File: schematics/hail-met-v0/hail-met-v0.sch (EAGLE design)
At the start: 87 parts, among them IC1 MCP73871, J1 AVR_SPI_PRG_6PTH, U1 ATMEGA328P, Y1 16MHZ

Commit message: finished initial schematic and routing, updated software pin assignment
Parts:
- removed ATM_PB, ATM_PC, ATM_PD, ATM_PWR, JP4: (no value), SparkFun-Connectors:M08LOCK
- removed LED7-FREE: M02PTH, SparkFun-Connectors:M02PTH
- added AND-GATE: SN74ALVC08PWR, Texas Instruments_By_element14_Batch_1:SN74ALVC08PWR
- added AT_PINS: M04X2, SparkFun-Connectors:M04X2
- added JP-BT1, JP-BT2, JP-BT3: (no value), SparkFun-Connectors:M04LOCK
- added LED7-CS, LED_CHG, LED_DONE, LED_LB, SW_BSEL1, SW_BSEL2, SW_TL1, SW_TR1: M02PTH, SparkFun-Connectors:M02PTH
- added NOT-GATE: SN74LVC3G14DCTR, Texas Instruments_By_element14_Batch_1:SN74LVC3G14DCTR
- added R14, R15: (no value), SparkFun-Passives:RESISTOR0805-RES
- renumbered JP3 to JP-BT0
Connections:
- net CHG_PWR renamed N$29
- removed net A: U1.PC1(ADC1)
- removed net B: U1.PC2(ADC2)
- removed net BT_DISC: U1.PD4(XCK/T0)
- removed net BT_GPIO10: JP4.8, U$3.GPIO10
- removed net BT_GPIO2: JP4.1
- removed net BT_GPIO5: JP4.4, U$3.GPIO5
- removed net BT_GPIO9: JP4.7
- removed net BT_PAIR: U1.PD7(AIN1)
- removed net C: U1.PC3(ADC3)
- removed net N$15: ATM_PC.1, ATM_PD.1
- removed net N$16: ATM_PC.2, ATM_PD.2
- removed net N$23: DONE.A, R5.1
- removed net N$26: ATM_PC.3, ATM_PD.3
- removed net N$32: ATM_PC.4, ATM_PD.4
- removed net N$34: U1.ADC7
- removed net N$43: ATM_PC.5, ATM_PD.5, ATM_PWR.5
- removed net N$45: ATM_PC.6, ATM_PD.6, ATM_PWR.6
- removed net N$46: ATM_PC.7, ATM_PD.7, ATM_PWR.7
- removed net N$47: ATM_PC.8, ATM_PD.8, ATM_PWR.8
- removed net N$48: ATM_PB.1
- removed net N$49: ATM_PB.2
- removed net N$50: ATM_PB.3
- removed net N$51: ATM_PB.4
- removed net N$52: ATM_PB.5
- removed net N$53: ATM_PB.6
- removed net N$54: ATM_PB.7
- removed net N$55: ATM_PB.8
- removed net N$67: LED_CREE.2, R24.1
- removed net SW_BFF: SW_BFF.1
- removed net SW_BRR: SW_BRR.1
- removed net SW_BSEL: SW_BSEL.1
- new net ADC6: AT_PINS.2, U1.ADC6
- new net ADC7: AT_PINS.4, U1.ADC7
- new net BT_NEXT: SW_BSEL1.1, U$3.GPIO11
- new net BT_PLAY: SW_BSEL.1, U$3.GPIO13
- new net BT_PREV: SW_BSEL2.1, U$3.GPIO12
- new net BT_USBD+: JP-BT1.3, U$3.USBD+
- new net BT_USBD-: JP-BT1.2, U$3.USBD-
- new net BT_VOL_DN: SW_BRR.1, U$3.GPIO10
- new net BT_VOL_UP: SW_BFF.1, U$3.GPIO5
- new net CHG_CHARGING: AND-GATE.4Y, LED_CHG.1
- new net CHG_LOWBATT: AND-GATE.3Y, LED_LB.1
- new net CHG_PG: AND-GATE.3B, NOT-GATE.3A, PWR.A, R6.1
- new net CHG_STAT2: AND-GATE.2B, DONE.A, NOT-GATE.2A, R5.1
- new net N$20: CHRG/LBO.C, IC1.STAT1/LBO
- new net N$28: DONE.C, IC1.STAT2
- new net N$30: LED_CHG.2, R24.1
- new net PC1: AT_PINS.3, U1.PC1(ADC1)
- new net PC2: AT_PINS.5, U1.PC2(ADC2)
- new net PC3: AT_PINS.7, U1.PC3(ADC3)
- new net STAT12: AND-GATE.2Y, AND-GATE.3A, AND-GATE.4A
- new net SW_BT_DISC: SW_TL1.1, U1.PD4(XCK/T0)
- new net SW_CALL: SW_TR1.1
- new net ~CHG_PG: AND-GATE.4B, NOT-GATE.3Y
- new net ~CHG_STAT1: AND-GATE.2A, NOT-GATE.1Y
- new net ~CHG_STAT2: AND-GATE.1B, NOT-GATE.2Y
- net 3.3V: now also AND-GATE.VCC, AT_PINS.1, JP-BT2.4, LED7-CS.1, NOT-GATE.VCC, R13.2, R5.2, R6.2; no longer LED7-FREE.1
- net AMB_IN: now also U1.PC0(ADC0); no longer U1.ADC6
- net BT_CONN: now also U1.PD7(AIN1); no longer U1.PD5(T1)
- net BT_GPIO3: now also JP-BT1.1; no longer JP4.2
- net BT_GPIO4: now also JP-BT2.1; no longer JP4.3
- net BT_GPIO6: now also JP-BT2.2; no longer JP4.5
- net BT_GPIO7: now also JP-BT2.3; no longer JP4.6
- net CHG_DONE: now also AND-GATE.1Y, LED_DONE.1; no longer DONE.C, IC1.STAT2
- net CHG_STAT1: now also AND-GATE.1A, CHRG/LBO.A, NOT-GATE.1A, R13.1; no longer CHRG/LBO.C, IC1.STAT1/LBO
- net CHG_VOUT: now also JP-BT3.1; no longer ATM_PWR.1, C7.1, U$1.IN
- net EXT_5V: now also JP-BT3.3; no longer ATM_PWR.3
- net GND: now also AND-GATE.GND, AT_PINS.6, AT_PINS.8, JP-BT1.4, JP-BT3.4, NOT-GATE.GND, R14.2, R15.2, R24.2, SW_BSEL1.2, SW_BSEL2.2, SW_TL1.2, SW_TR1.2; no longer ATM_PWR.4
- net LED_CREE: now also U1.PD5(T1); no longer U1.PC0(ADC0)
- net N$19: now also LED_CREE.2; no longer R24.2
- net N$22: now also LED_DONE.2, R14.1; no longer CHRG/LBO.A, R13.1
- net N$24: now also LED_LB.2, R15.1; no longer PWR.A, R6.1
- net N$61: now also LED7-CS.2; no longer LED7-FREE.2
- net VCHG: no longer R13.2, R5.2, R6.2
- net VIN: now also C7.1, JP-BT3.2, U$1.IN; no longer ATM_PWR.2
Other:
- note added: "A0"
- note added: "A1"
- note added: "A2"
- note added: "A3"
- note added: "A4"
- note added: "A5"
- note added: "Breakout for ATmega328P"
- note added: "D0"
- note added: "D1"
- note added: "D10"
- note added: "D11"
- note added: "D12"
- note added: "D13"
- note added: "D2"
- note added: "D3"
- note added: "D4"
- note added: "D5"
- note added: "D6"
- note added: "D7"
- note added: "D8"
- note added: "D9"
- note added: "Logic for charge status LEDs"
- note added: "Names: ------ LED0-LF Left Front LED0-IL Indicator Left LED1-LM Left Middle LED2-LR Left Rear LED3-HR Headlight Rear LED4-RF Right Front LED4-IR Indicator Right LED5-RM Right Middle LED6-RR Right Rear LED7-CS Call Status"
- note added: "Names: ------ SW_TL Turn Left SW_TR Turn Right SW_BT_DISC Bluetooth Discoverable SW_CALL Accept/Reject call"
- note added: "See Fig 2-4 for usage http://ww1.microchip.com/downloads/ en/DeviceDoc/rn-52-ds-1.1r.pdf"
- note added: "x"
- note removed: "Breakout for ATmega328"
- note removed: "Do we need these jumpers?"
- note removed: "Names: ------ LED0-LF Left Front LED0-IL Indicator Left LED1-LM Left Middle LED2-LR Left Rear LED3-HR Headlight Front LED4-RF Right Front LED4-IR Indicator Right LED5-RM Right Middle LED6-RR Right Rear LED7-FREE"
- note removed: "Names: ------ SW-TL Turn Left SW-TR Turn Right SW-BFF Bluetooth Fast Forward SW-BRR Bluetooth Rewind SW-BSEL Bluetooth Select"
- note removed: "Note: Processor pins do not match button pins yet, and pins and there is 1 less pin than expected. ADC6/ ADC7 were factored in as pins, but not on standard Arduino IDE(?)"
- moved on the sheet: C1, CHRG/LBO, DONE, FTDI, J1, LED0-IL, LED0-IR, LED0-LF, LED1-LM, LED2-LR, LED3-HR, LED4-RF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

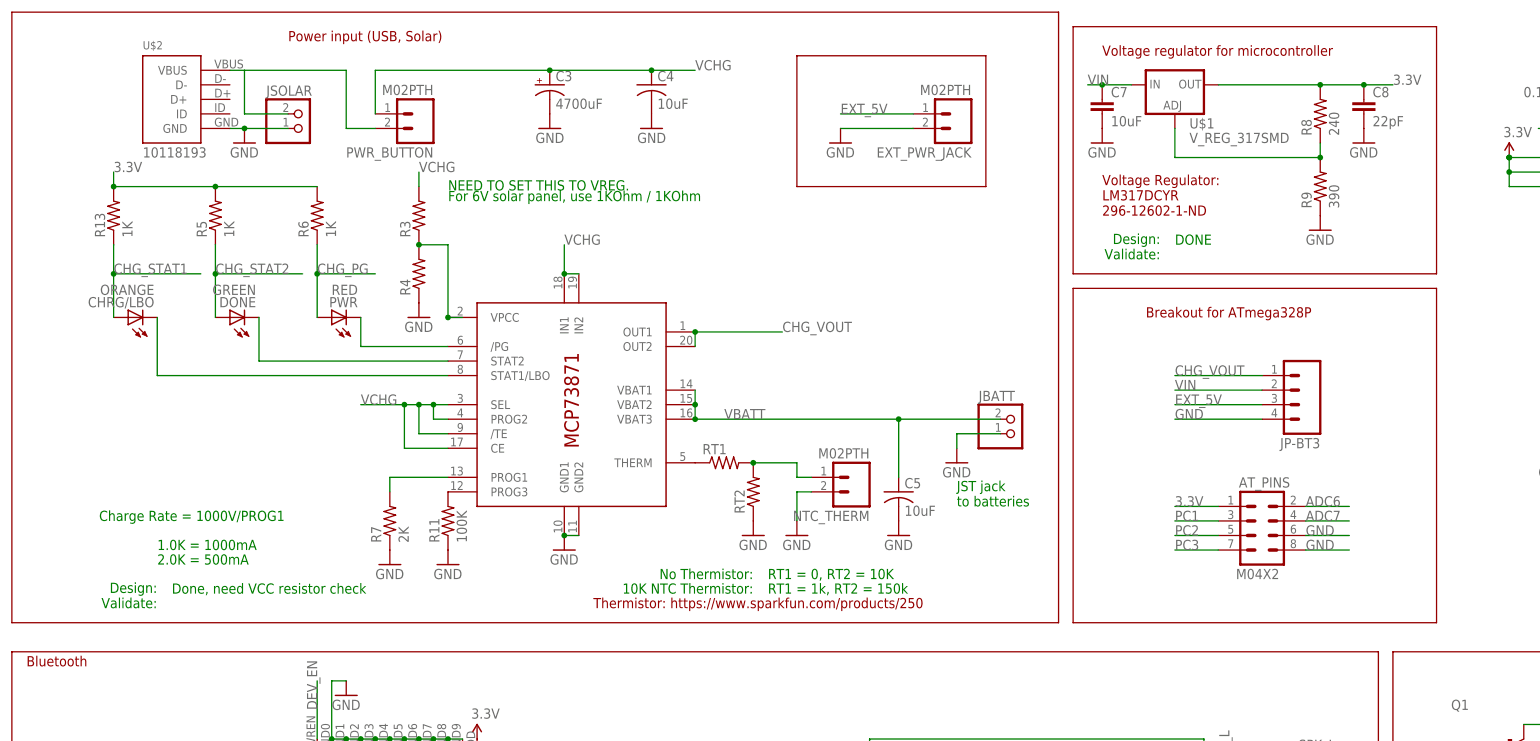
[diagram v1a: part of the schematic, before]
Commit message: added some power planes
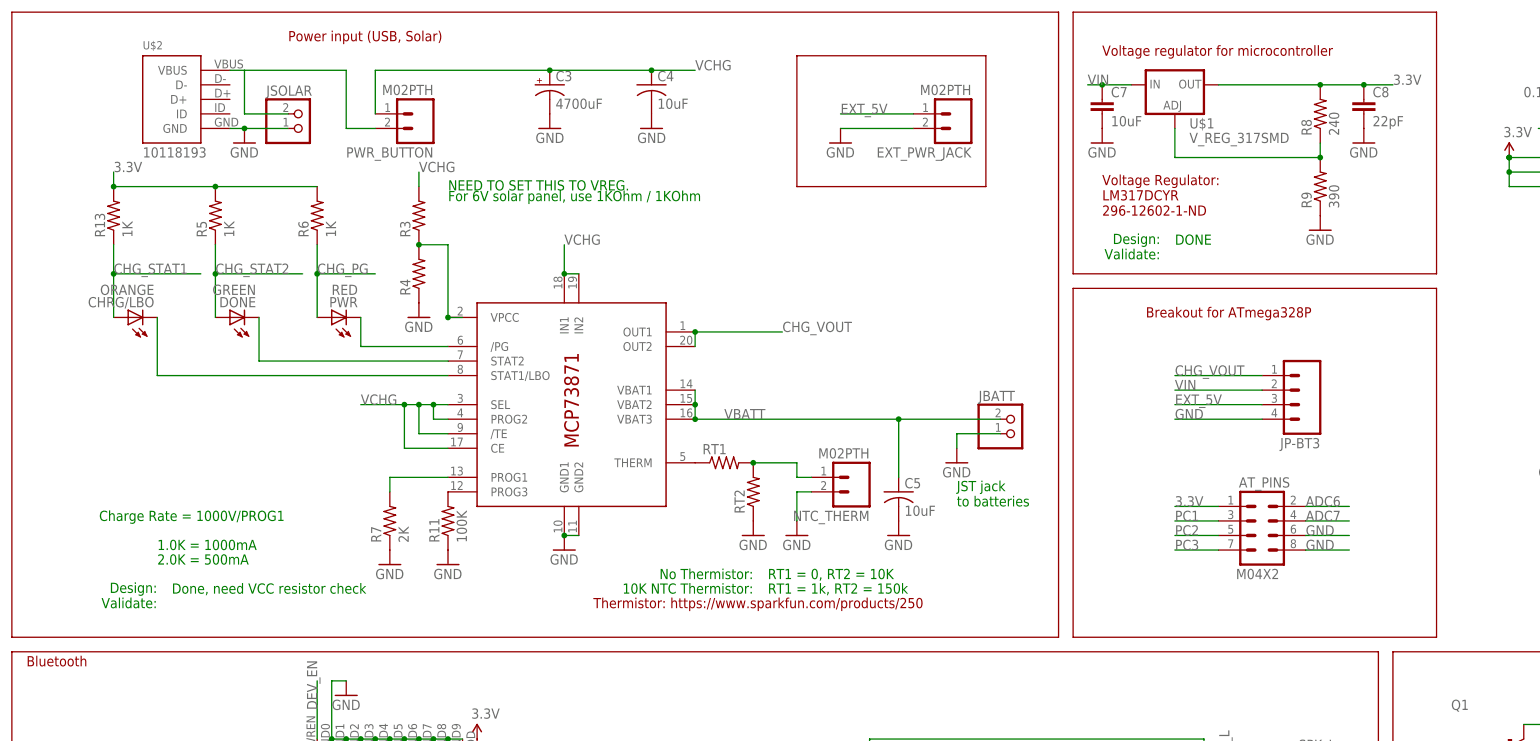
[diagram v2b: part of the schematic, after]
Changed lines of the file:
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@@
 <text x="2.54" y="96.52" size="1.778" layer="94">Voltage regulator for microcontroller</text>
 <text x="81.28" y="-33.02" size="1.778" layer="94">LED Driver</text>
-<wire x1="-187.96" y1="104.14" x2="-187.96" y2="-2.54" width="0.1524" layer="94"/>
-<wire x1="-187.96" y1="-2.54" x2="-5.08" y2="-2.54" width="0.1524" layer="94"/>
-<wire x1="-5.08" y1="-2.54" x2="-5.08" y2="104.14" width="0.1524" layer="94"/>
+<wire x1="-187.96" y1="104.14" x2="-187.96" y2="-5.08" width="0.1524" layer="94"/>
+<wire x1="-187.96" y1="-5.08" x2="-5.08" y2="-5.08" width="0.1524" layer="94"/>
+<wire x1="-5.08" y1="-5.08" x2="-5.08" y2="104.14" width="0.1524" layer="94"/>
 <wire x1="-5.08" y1="104.14" x2="-187.96" y2="104.14" width="0.1524" layer="94"/>
 <text x="-139.7" y="99.06" size="1.778" layer="94">Power input (USB, Solar)</text>
@@
 For 6V solar panel, use 1KOhm / 1KOhm</text>
 <text x="15.24" y="63.5" size="1.778" layer="91">DONE</text>
-<wire x1="-2.54" y1="101.6" x2="60.96" y2="101.6" width="0.1524" layer="94"/>
-<wire x1="60.96" y1="101.6" x2="60.96" y2="58.42" width="0.1524" layer="94"/>
+<wire x1="-2.54" y1="104.14" x2="60.96" y2="104.14" width="0.1524" layer="94"/>
+<wire x1="60.96" y1="104.14" x2="60.96" y2="58.42" width="0.1524" layer="94"/>
 <wire x1="60.96" y1="58.42" x2="-2.54" y2="58.42" width="0.1524" layer="94"/>
-<wire x1="-2.54" y1="58.42" x2="-2.54" y2="101.6" width="0.1524" layer="94"/>
+<wire x1="-2.54" y1="58.42" x2="-2.54" y2="104.14" width="0.1524" layer="94"/>
 <text x="12.7" y="60.96" size="1.778" layer="91" align="bottom-right">Design:
 Validate:</text>
@@
 <wire x1="304.8" y1="-101.6" x2="304.8" y2="-7.62" width="0.1524" layer="94"/>
 <wire x1="304.8" y1="-7.62" x2="223.52" y2="-7.62" width="0.1524" layer="94"/>
-<wire x1="-2.54" y1="55.88" x2="-2.54" y2="-2.54" width="0.1524" layer="94"/>
-<wire x1="-2.54" y1="-2.54" x2="60.96" y2="-2.54" width="0.1524" layer="94"/>
-<wire x1="60.96" y1="-2.54" x2="60.96" y2="55.88" width="0.1524" layer="94"/>
+<wire x1="-2.54" y1="55.88" x2="-2.54" y2="-5.08" width="0.1524" layer="94"/>
+<wire x1="-2.54" y1="-5.08" x2="60.96" y2="-5.08" width="0.1524" layer="94"/>
+<wire x1="60.96" y1="-5.08" x2="60.96" y2="55.88" width="0.1524" layer="94"/>
 <wire x1="60.96" y1="55.88" x2="-2.54" y2="55.88" width="0.1524" layer="94"/>
 <text x="10.16" y="50.8" size="1.778" layer="94">Breakout for ATmega328P</text>

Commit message: routing pcb
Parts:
- removed JP-BT0: (no value), SparkFun-Connectors:M08LOCK
- added D2: (no value), adafruit:DIODESOD-123
- added LED_BTCONN: M02PTH, SparkFun-Connectors:M02PTH
- added R25: (no value), SparkFun-Passives:RESISTOR0805-RES
- added R26, R27, R28: 1K, SparkFun-Passives:RESISTOR0805-RES
- NOT-GATE: value SN74LVC3G14DCTR -> SN74AUP3G04DQER; device Texas Instruments_By_element14_Batch_1:SN74LVC3G14DCTR -> Texas Instruments_By_element14_Batch_1:SN74AUP3G04DQER
- R13, R5, R6: value 1K -> 10K
- renumbered SW_BFF to SW_VUP, SW_BRR to SW_VDN, SW_BSEL to SW_PLAY, SW_BSEL1 to SW_NEXT, SW_BSEL2 to SW_PREV, SW_TL1 to SW_DISC, SW_TR1 to SW_CALL
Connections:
- removed net N$25: U1.AREF
- removed net N$28: DONE.C, IC1.STAT2
- removed net N$29: IC1./PG, PWR.C
- removed net N$73: CI_L.2, U$3.SPKR_L+
- removed net N$76: CI_R.2, U$3.SPKR_R+
- removed net PC3: AT_PINS.7, U1.PC3(ADC3)
- removed net SPKR_L-: JP-BT0.3
- removed net SPKR_R-: JP-BT0.4
- new net AREF: AT_PINS.3, U1.AREF
- new net N$15: D2.A, JSOLAR.1
- new net N$16: LED_BTCONN.2, R25.1
- new net N$23: PWR.A, R28.1
- net 3.3V: now also R26.2, R27.2, R28.2
- net BT_CONN: now also LED_BTCONN.1
- net CHG_PG: now also IC1./PG, PWR.C; no longer PWR.A
- net CHG_STAT1: now also CHRG/LBO.C, IC1.STAT1/LBO; no longer CHRG/LBO.A
- net CHG_STAT2: now also DONE.C, IC1.STAT2; no longer DONE.A
- net GND: now also R25.2, U$3.AGND
- net MIC_L+: no longer JP-BT0.8
- net MIC_L-: no longer JP-BT0.6
- net MIC_R+: no longer JP-BT0.7
- net MIC_R-: no longer JP-BT0.5
- net N$20: now also CHRG/LBO.A, R26.1; no longer CHRG/LBO.C, IC1.STAT1/LBO
- net N$21: now also DONE.A, R27.1; no longer J1.2
- net N$80: now also D2.C; no longer JSOLAR.1
- net PC1: now also AT_PINS.5; no longer AT_PINS.3
- net PC2: now also AT_PINS.7; no longer AT_PINS.5
- net SPKR_L+: now also CI_L.2, U$3.SPKR_L+; no longer JP-BT0.1
- net SPKR_R+: now also CI_R.2, U$3.SPKR_R+; no longer JP-BT0.2
- net SW_CALL: now also U1.PC3(ADC3)
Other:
- moved on the sheet: CHRG/LBO, DONE, PWR, U$2
